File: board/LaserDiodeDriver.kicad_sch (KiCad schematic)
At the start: 63 parts, among them K3 EE2-12NUH, Q2 FQP27P06, Q8 FQP27P06, U1 OPA4192, U2 LT1009xZ, U20 OPA4192, U3 OP77, U4 LM317_SOT-223, U5 LT1009xZ, U7 OP77, U9 OPA4192

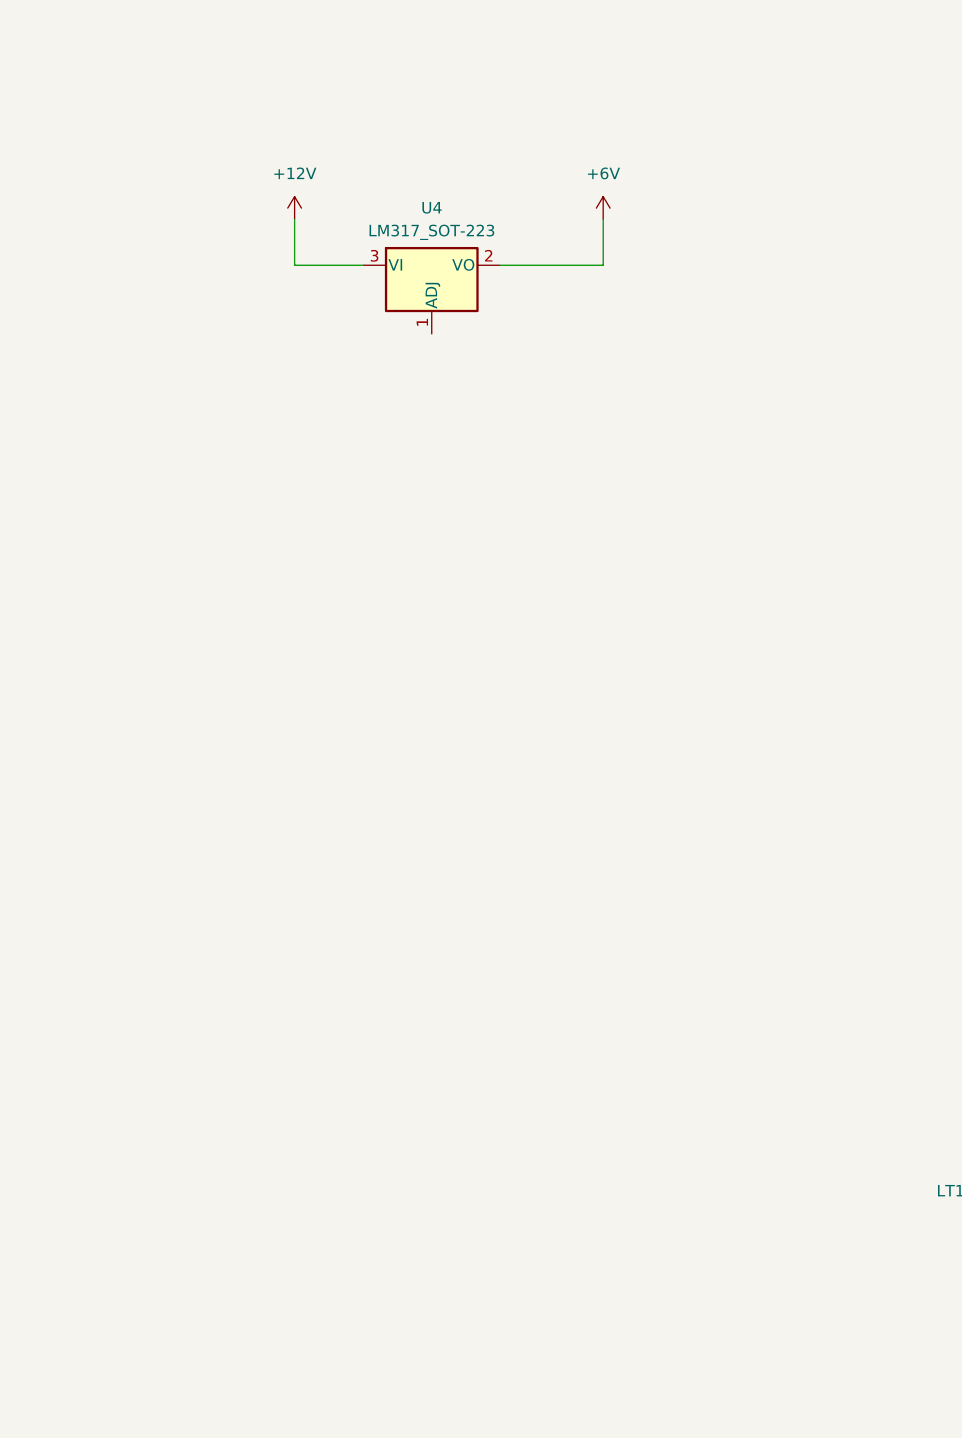
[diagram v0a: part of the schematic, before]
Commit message: Made/tested LM317 circuit
The LM317 was configured for 12V input and 6V output to power the main laser driver circuit. With a high power LED as a stand in for the laser diode and current set to 125mA, the power dissipation of the LM317 was high enough for a heat sink to be necessary with a fan. This is not ideal so a 6V buck will be looked into. If that cannot be found, maybe it's worth trying other voltages and weighing the tradeoffs of heat dissipation in the control FET vs the regulator.
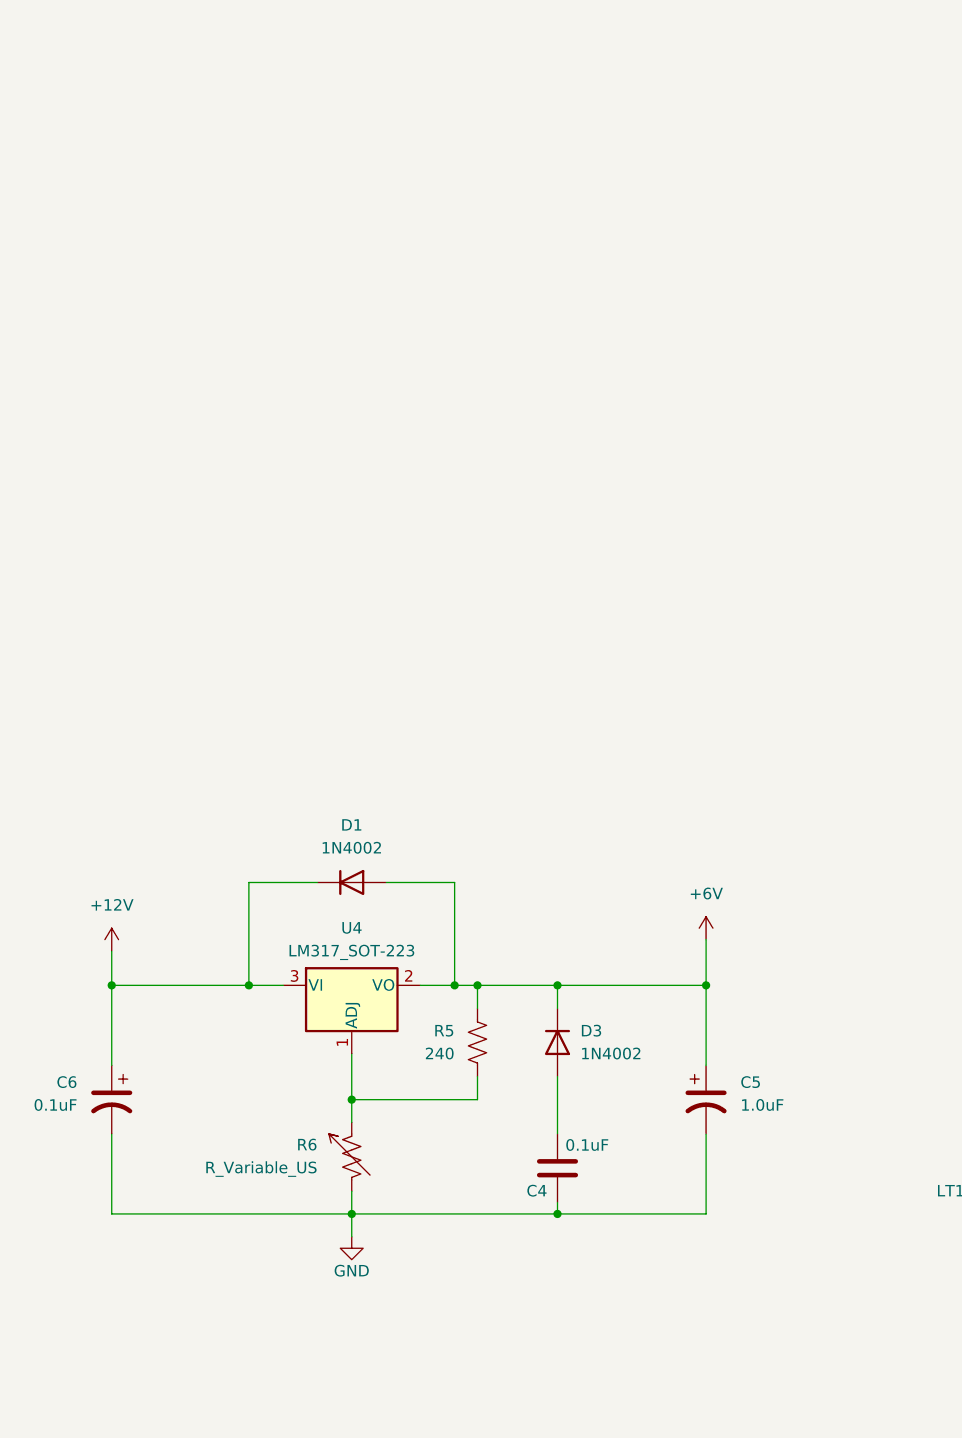
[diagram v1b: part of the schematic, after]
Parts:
- added C4: 0.1uF, symbol Device:C
- added C5: 1.0uF, symbol Device:C_Polarized_US
- added C6: 0.1uF, symbol Device:C_Polarized_US
- added D1, D3: 1N4002, Diode_THT:D_DO-41_SOD81_P10.16mm_Horizontal, symbol Diode:1N4002
- added R5: 240, symbol Device:R_US
- added R6: R_Variable_US, symbol Device:R_Variable_US
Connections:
- net +12V: now also C6.1, D1.1 (K)
- net +6V: now also C5.1, D1.2 (A), D3.1 (K), R5.1
- net GND: now also C4.2, C5.2, C6.2, R6.2
- net at U4.1 (ADJ): now also R5.2, R6.1
- new net: C4.1, D3.2 (A)
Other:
- moved on the sheet: U4

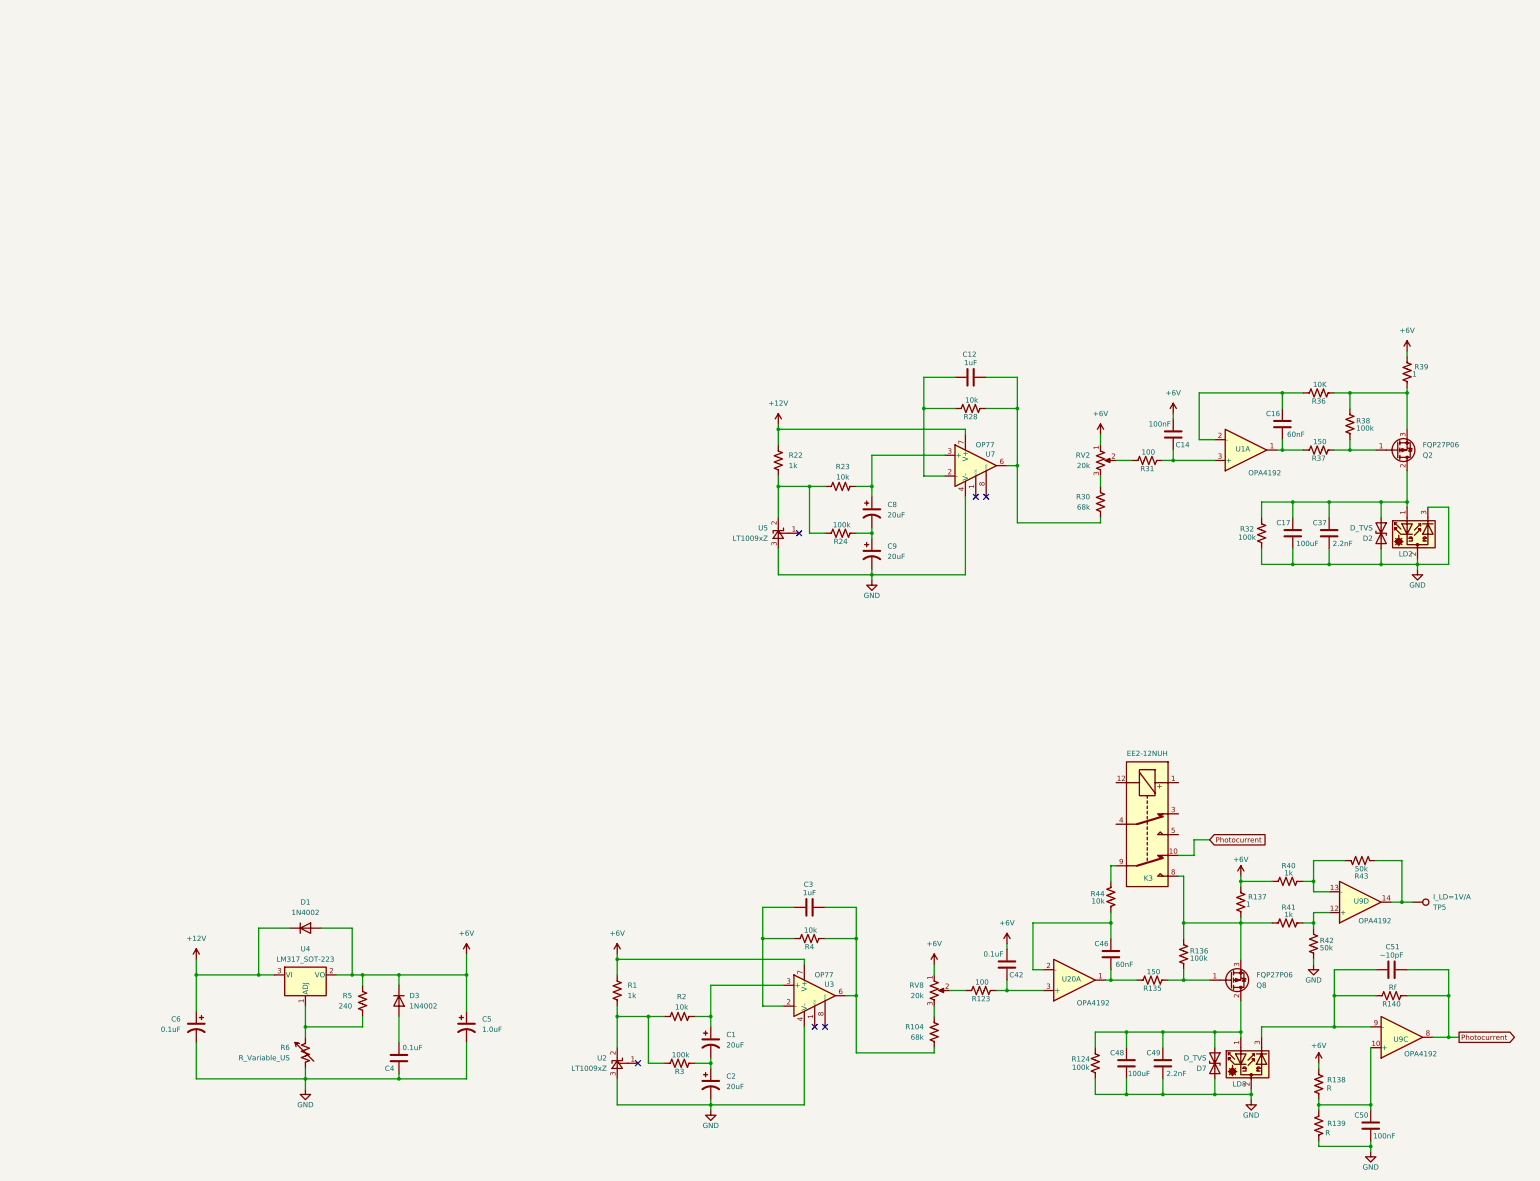
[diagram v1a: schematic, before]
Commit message: Various changes (read description for info)
* Changed LM317 output voltage to be 10V since testing at that voltage reduced heat dissipation across shunt, LM317, and current drive FET.
* Deleted test schematic
* Swapped 1Ohm shunt to five 5Ohm SMD resistors with +_50ppm/*C at 1% tolerance to distribute heat load and average out tolerances.
* Found proper quad symbol for OP-amp and inserted datasheet + footprint.
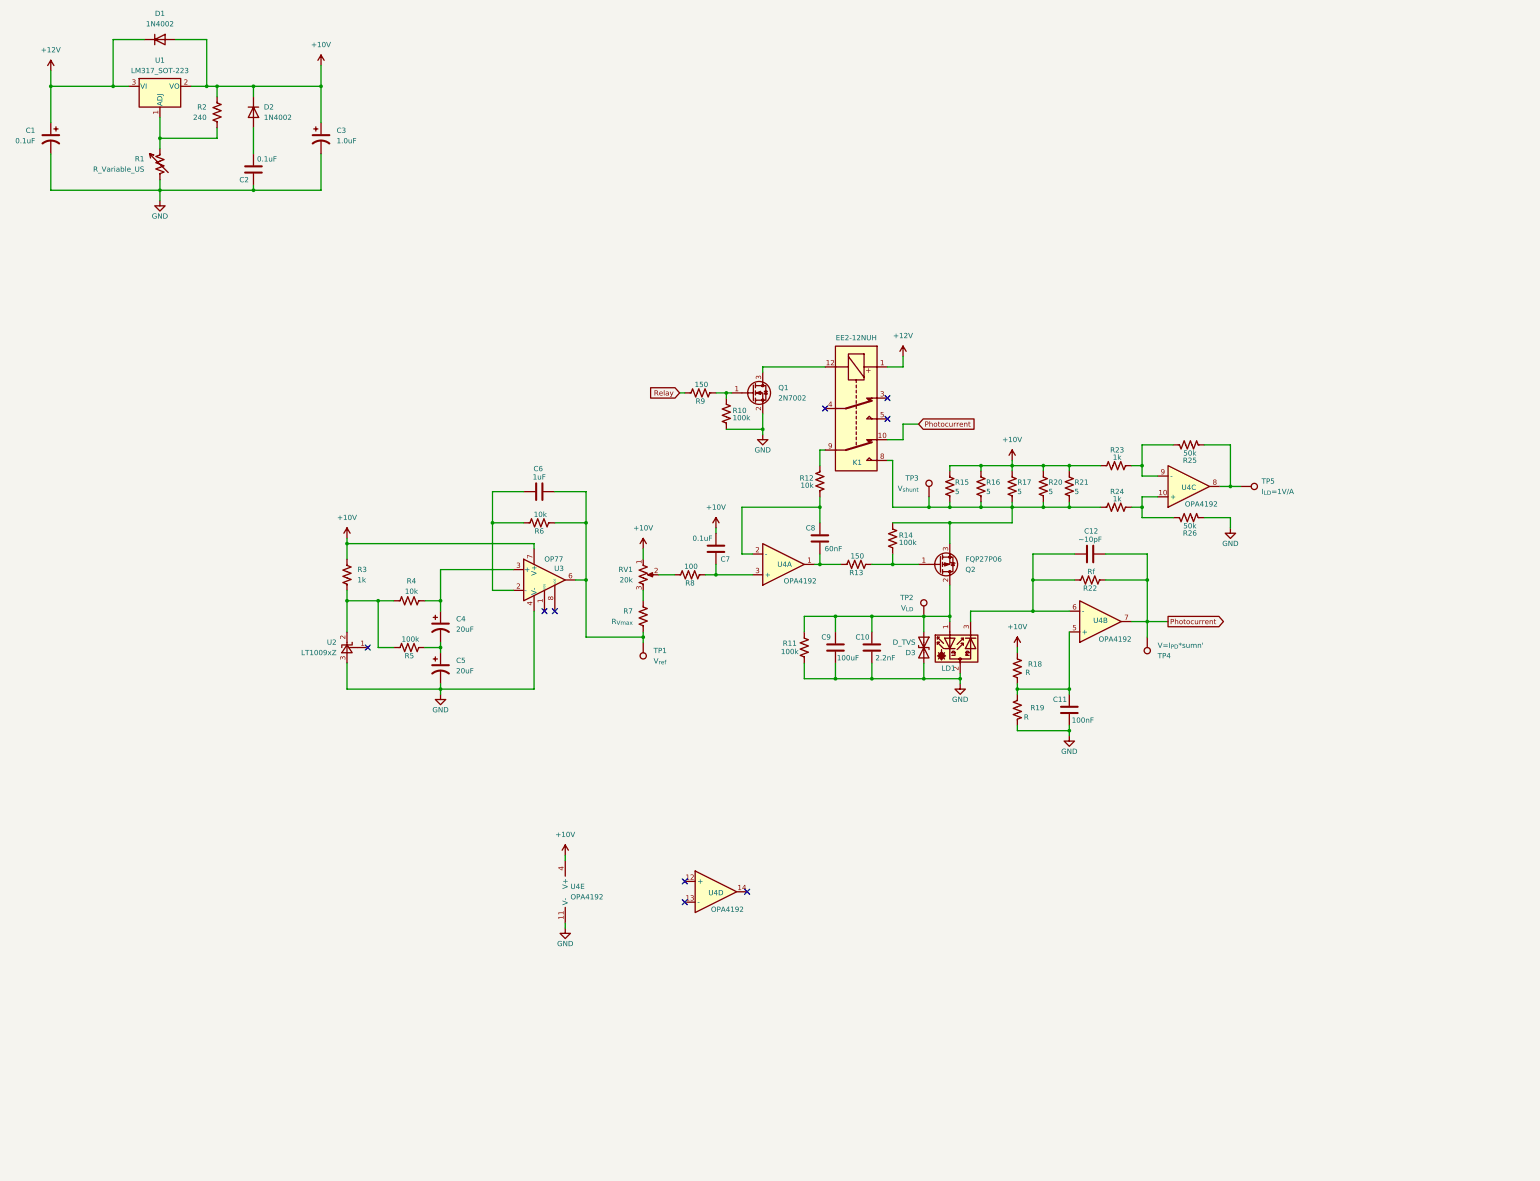
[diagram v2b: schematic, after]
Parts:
- removed C12: 1uF, symbol Device:C
- removed C14: 100nF, symbol Device:C
- removed C16: 60nF, symbol Device:C
- removed C17: 100uF, symbol Device:C
- removed C37: 2.2nF, symbol Device:C
- removed C8, C9: 20uF, symbol Device:C_Polarized_US
- removed D2: D_TVS, symbol Device:D_TVS
- removed LD2: L785P090, symbol Device:D_Laser_Photo_PType
- removed Q2: FQP27P06, Package_TO_SOT_THT:TO-220-3_Vertical, symbol Transistor_FET:FQP27P06
- removed R137, R39: 1, symbol Device:R_US
- removed R22: 1k, symbol Device:R_US
- removed R23, R28: 10k, symbol Device:R_US
- removed R24, R32, R38: 100k, symbol Device:R_US
- removed R30: 68k, symbol Device:R_US
- removed R31: 100, symbol Device:R_US
- removed R36: 10K, symbol Device:R_US
- removed R37: 150, symbol Device:R_US
- removed R42: 50k, symbol Device:R_US
- removed RV2: 20k, symbol Device:R_Potentiometer_US
- removed U1, U20: OPA4192, Package_SO:SOIC-14_3.9x8.7mm_P1.27mm, symbol Amplifier_Operational:MCP6004
- removed U5: LT1009xZ, Package_TO_SOT_THT:TO-92L_Inline, symbol Reference_Voltage:LT1009xZ
- removed U7: OP77, symbol Amplifier_Operational:OP77
- removed U9: OPA4192, symbol Amplifier_Operational:MCP6004
- added Q1: 2N7002, Package_TO_SOT_SMD:SOT-23, symbol Transistor_FET:2N7002
- added R10: 100k, symbol Device:R_US
- added R15, R16, R17, R20, R21: 5, Resistor_SMD:R_2010_5025Metric_Pad1.40x2.65mm_HandSolder, symbol Device:R_US
- added R26: 50k, symbol Device:R_US
- added R9: 150, symbol Device:R_US
- added TP1: V_{ref}, symbol Connector:TestPoint
- added TP2: V_{LD}, symbol Connector:TestPoint
- added TP3: V_{shunt}, symbol Connector:TestPoint
- added TP4: V=I_{PD}*sumn', symbol Connector:TestPoint
- added U4: OPA4192, Package_SO:SOIC-14_3.9x8.7mm_P1.27mm, symbol Device:Opamp_Quad
- R7: renamed from R104; value 68k -> R_{Vmax}
- TP5: value I_LD=1V/A -> I_{LD}=1V/A
- renumbered C6 to C1, C49 to C10, C50 to C11, C51 to C12, C4 to C2, C5 to C3, C1 to C4, C2 to C5, C3 to C6, C42 to C7, C46 to C8, C48 to C9, D3 to D2, D7 to D3, K3 to K1, LD8 to LD1, Q8 to Q2, R6 to R1, R124 to R11, R44 to R12, R135 to R13, R136 to R14, R138 to R18, R139 to R19, R5 to R2, R140 to R22, R40 to R23, R41 to R24, R43 to R25, R1 to R3, R2 to R4, R3 to R5, R4 to R6, R123 to R8, RV8 to RV1, U4 to U1
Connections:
- net +12V: now also K1.1
- net GND: now also Q1.2 (S), R10.2, R26.2, U4.11 (V-)
- net Photocurrent: now also TP4.1, U4.7
- net at C6.2, R6.2, R7.2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: now also TP1.1
- net at R23.2, R25.1: now also U4.9 (-)
- net at R25.2, TP5.1: now also U4.8
- net at C10.2, C9.2, D3.1 (A1)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: now also TP2.1
- net at K1.8, Q2.3 (S), R14.1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: now also R15.2, R16.2, R17.2, R20.2, R21.2, TP3.1
- net at R24.2: now also R26.1, U4.10 (+)
- net at C12.2, LD1.3, R22.1: now also U4.6 (-)
- net at C8.1, R13.1: now also U4.1
- net at C8.2, R12.2: now also U4.2 (-)
- net at C7.2, R8.2: now also U4.3 (+)
- net at C11.2, R18.2, R19.1: now also U4.5 (+)
- net at K1.12: now also Q1.3 (D)
- net +6V renamed +10V
- net +10V: now also R15.1, R16.1, R17.1, R20.1, R21.1, U4.4 (V+)
- new net: Q1.1 (G), R10.1, R9.2
- new net Relay: R9.1
- no-connect marks 6 -> 9
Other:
- moved on the sheet: C1, C10, C11, C12, C2, C3, C4, C5, C6, C7, C8, C9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
